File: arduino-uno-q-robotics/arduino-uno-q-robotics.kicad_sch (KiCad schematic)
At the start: 15 parts, among them J1 Conn_02x30_Odd_Even, J2 Conn_02x30_Odd_Even, J3 Connector_FFC-FPC, J4 Connector_FFC-FPC, J5 Conn_02x13_Odd_Even, J6 Conn_02x04_Odd_Even, U1 LSM6DSO32, U2 TCA9803, U4 TCA9803

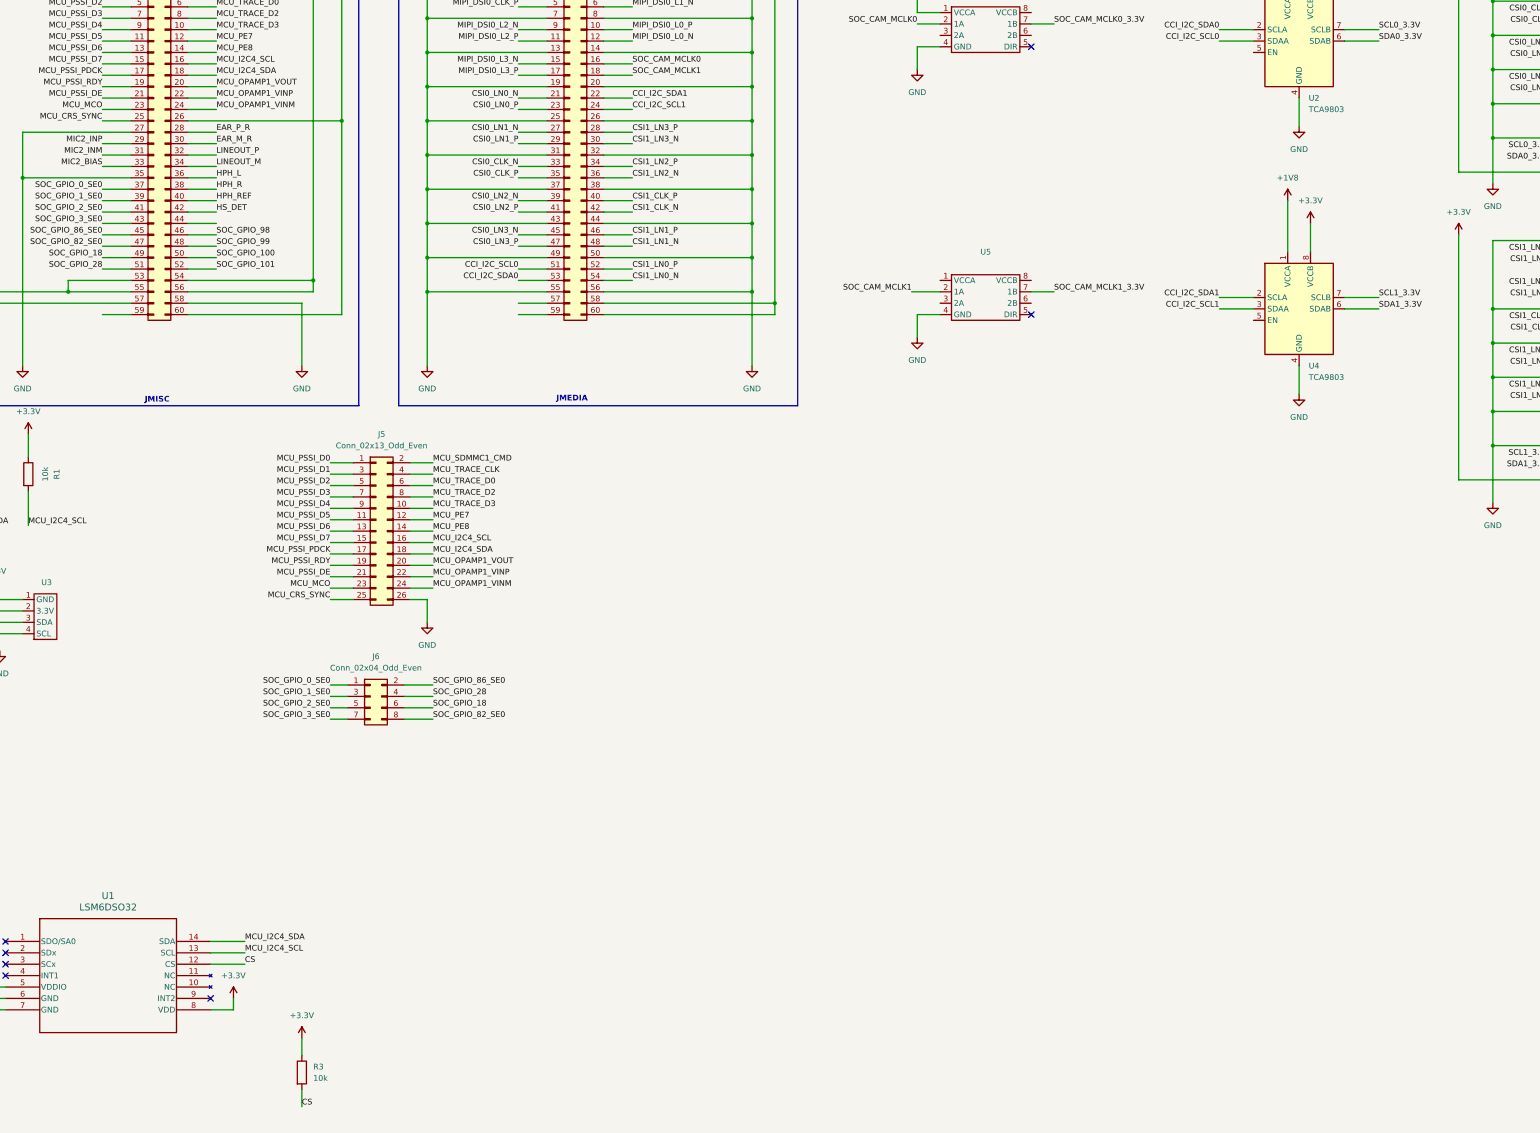
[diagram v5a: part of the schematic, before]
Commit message: Add decoupling capacitors to schematic
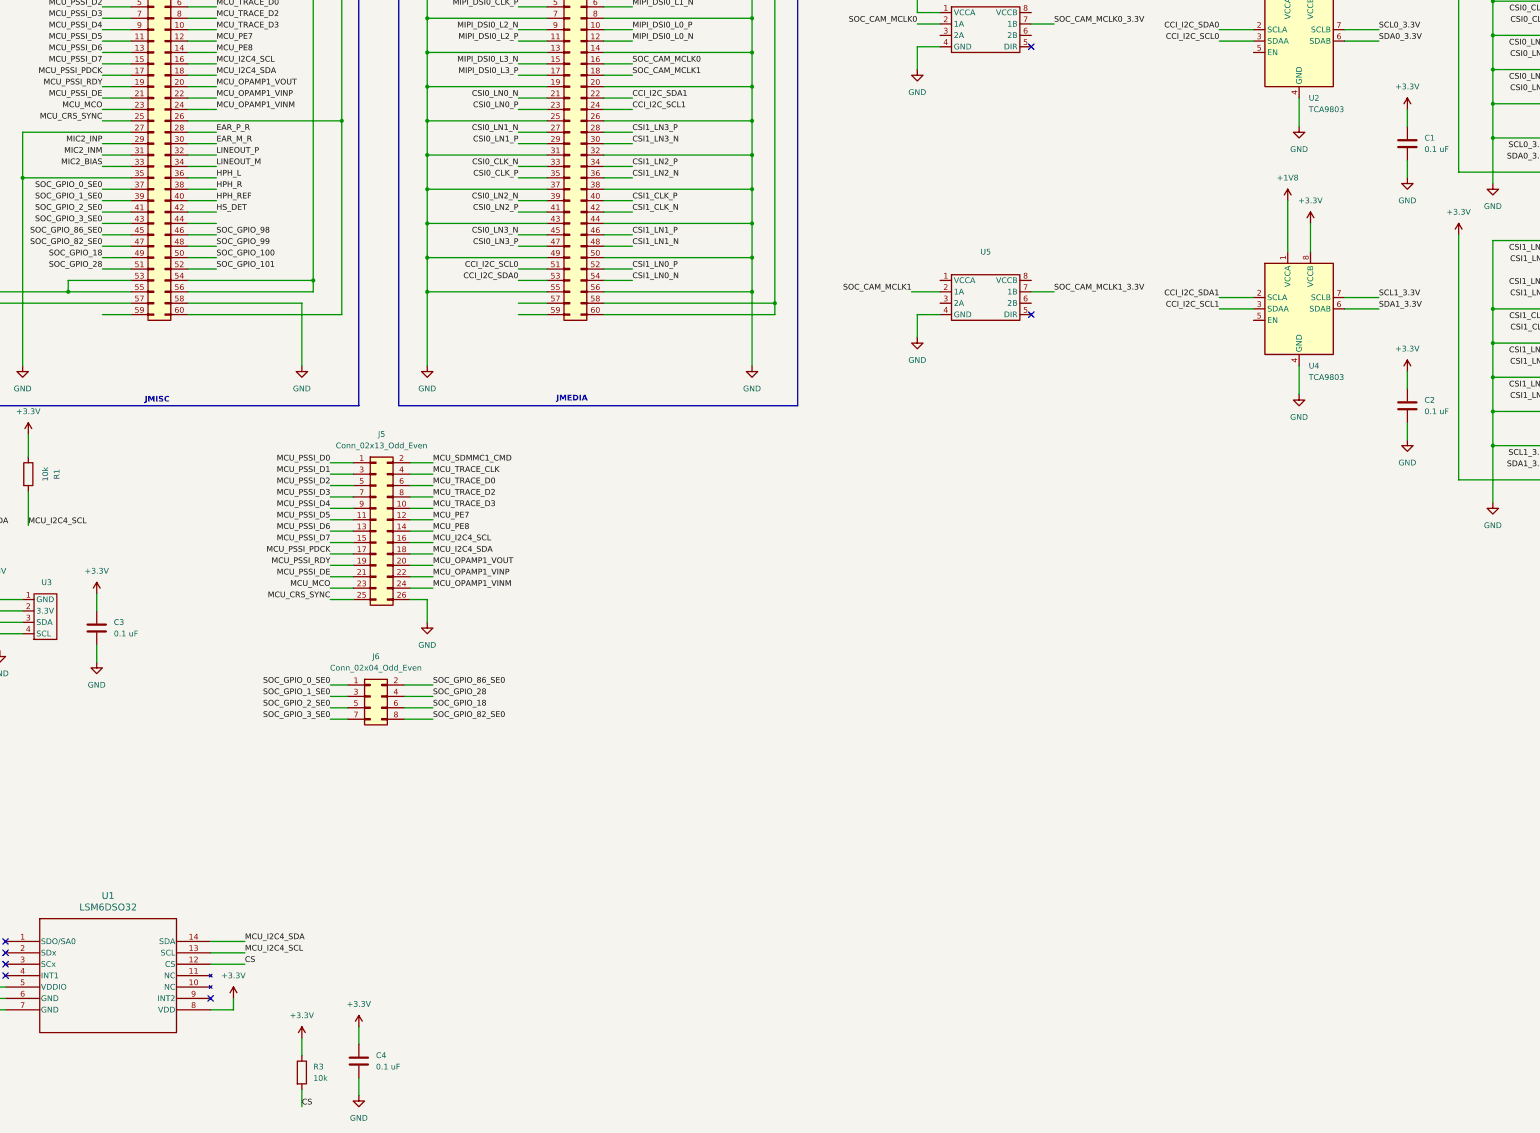
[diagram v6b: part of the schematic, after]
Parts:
- added C1, C2, C3, C4: 0.1 uF, Capacitor_SMD:C_0603_1608Metric_Pad1.08x0.95mm_HandSolder, symbol Device:C
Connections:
- net +3.3V: now also C1.1, C2.1, C3.1, C4.1
- net GND: now also C1.2, C2.2, C3.2, C4.2

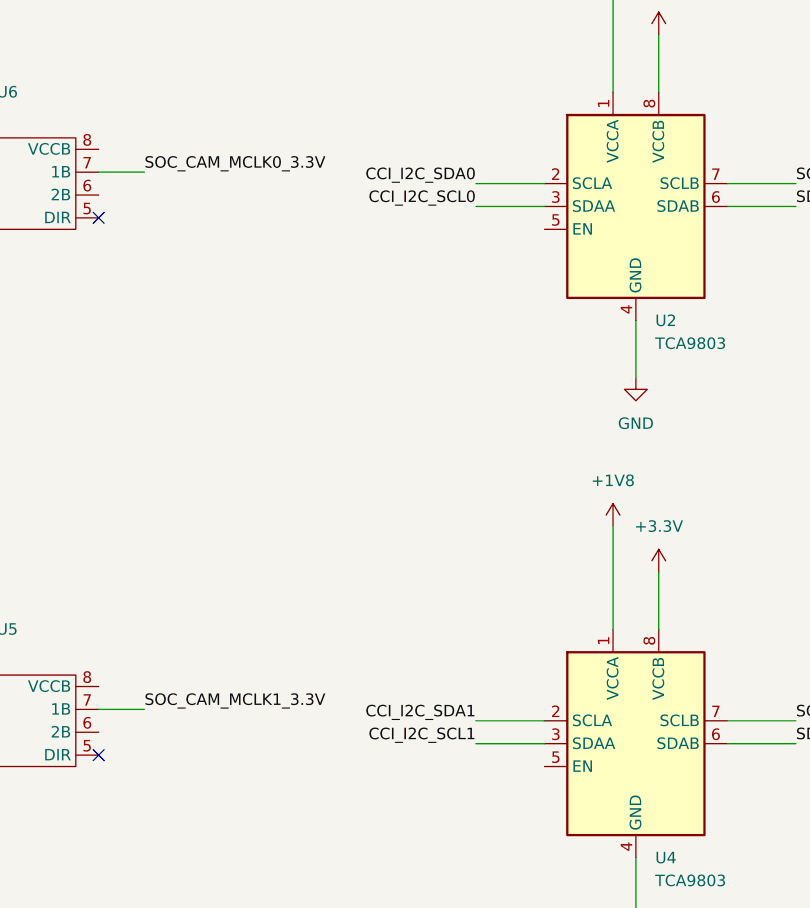
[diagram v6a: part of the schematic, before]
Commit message: Add missing components to PCB editor
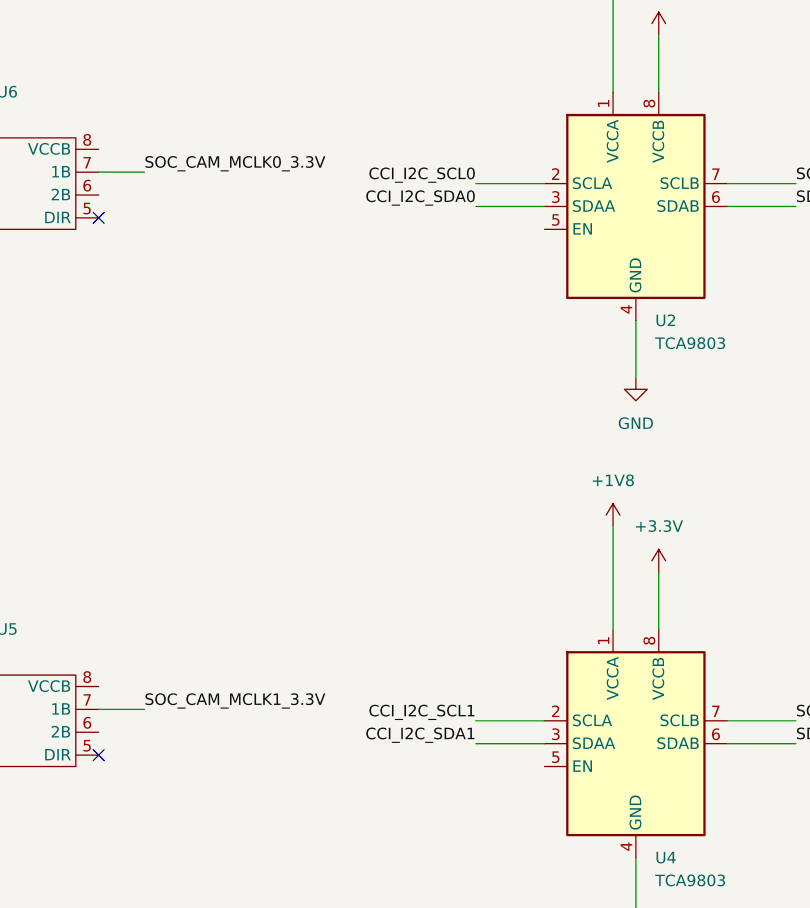
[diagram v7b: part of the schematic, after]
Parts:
- U1: footprint LGA-14L_2P5X3X0P83_STM -> robotics-footprints:LGA-14L_2P5X3X0P83_STM
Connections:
- net CCI_I2C_SCL0: now also U2.2 (SCLA); no longer U2.3 (SDAA)
- net CCI_I2C_SCL1: now also U4.2 (SCLA); no longer U4.3 (SDAA)
- net CCI_I2C_SDA0: now also U2.3 (SDAA); no longer U2.2 (SCLA)
- net CCI_I2C_SDA1: now also U4.3 (SDAA); no longer U4.2 (SCLA)
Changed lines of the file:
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@@
 		)
 	)
-	(label "CCI_I2C_SCL0"
-		(at 302.26 44.45 180)
-		(effects
-			(font
-				(size 1.27 1.27)
-			)
-			(justify right bottom)
-		)
-	)
 	(label "MCU_PSSI_D6"
 		(at 53.34 46.99 180)
@@
 	)
 	(label "CCI_I2C_SCL0"
+		(at 302.26 41.91 180)
+		(effects
+			(font
+				(size 1.27 1.27)
+			)
+			(justify right bottom)
+		)
+	)
+	(label "CCI_I2C_SCL0"
 		(at 146.05 95.25 180)
 		(effects
@@
 		)
 	)
+	(label "CCI_I2C_SDA0"
+		(at 302.26 44.45 180)
+		(effects
+			(font
+				(size 1.27 1.27)
+			)
+			(justify right bottom)
+		)
+	)
 	(label "SOC_GPIO_1_SE0"
 		(at 53.34 80.01 180)
@@
 		)
 	)
-	(label "CCI_I2C_SDA0"
-		(at 302.26 41.91 180)
-		(effects
-			(font
-				(size 1.27 1.27)
-			)
-			(justify right bottom)
-		)
-	)
 	(label "MCU_PSSI_PDCK"
 		(at 53.34 52.07 180)
@@
 		)
 	)
-	(label "CCI_I2C_SDA1"
+	(label "CCI_I2C_SCL1"
 		(at 302.26 101.6 180)
 		(effects
@@
 		)
 	)
-	(label "CCI_I2C_SCL1"
+	(label "CCI_I2C_SDA1"
 		(at 302.26 104.14 180)
 		(effects
@@
 			)
 		)
-		(property "Footprint" "LGA-14L_2P5X3X0P83_STM"
+		(property "Footprint" "robotics-footprints:LGA-14L_2P5X3X0P83_STM"
 			(at 56.642 268.224 0)
 			(effects

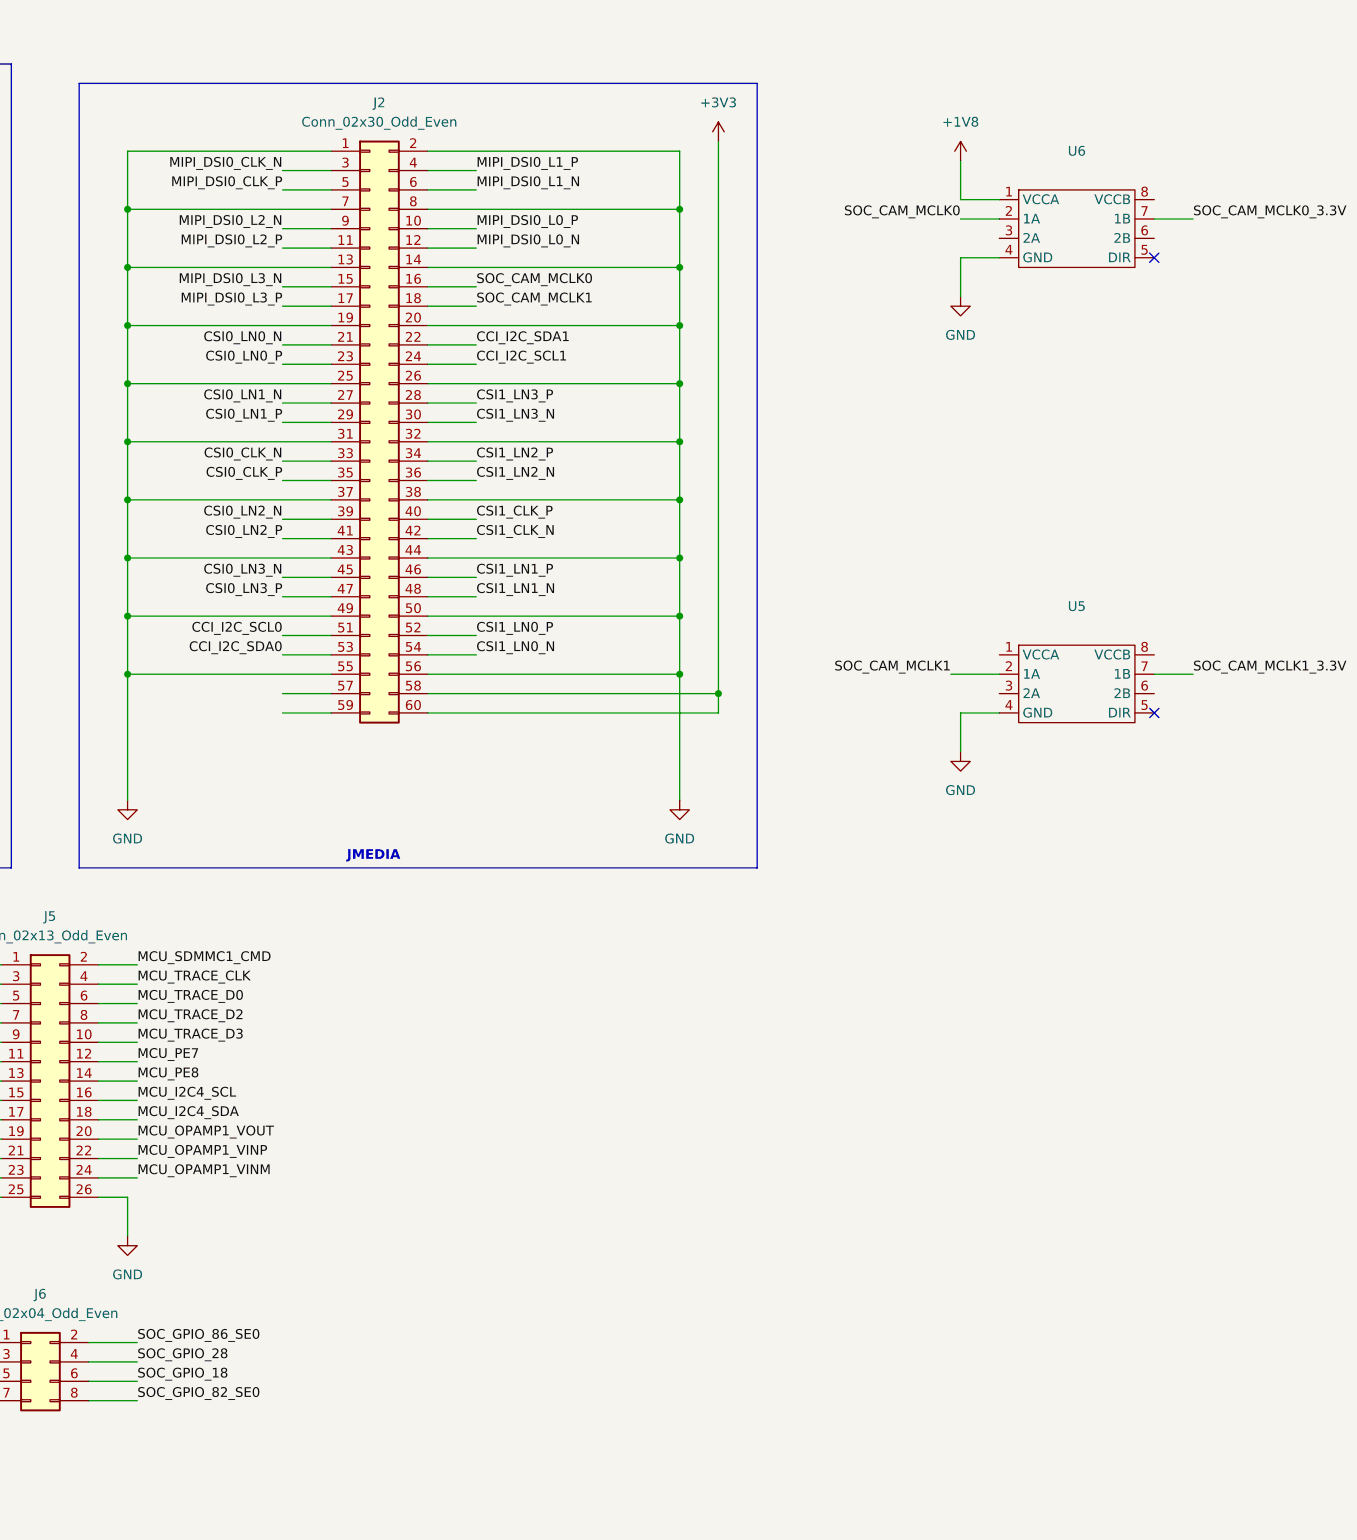
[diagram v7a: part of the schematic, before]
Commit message: Add male header for JMISC ports
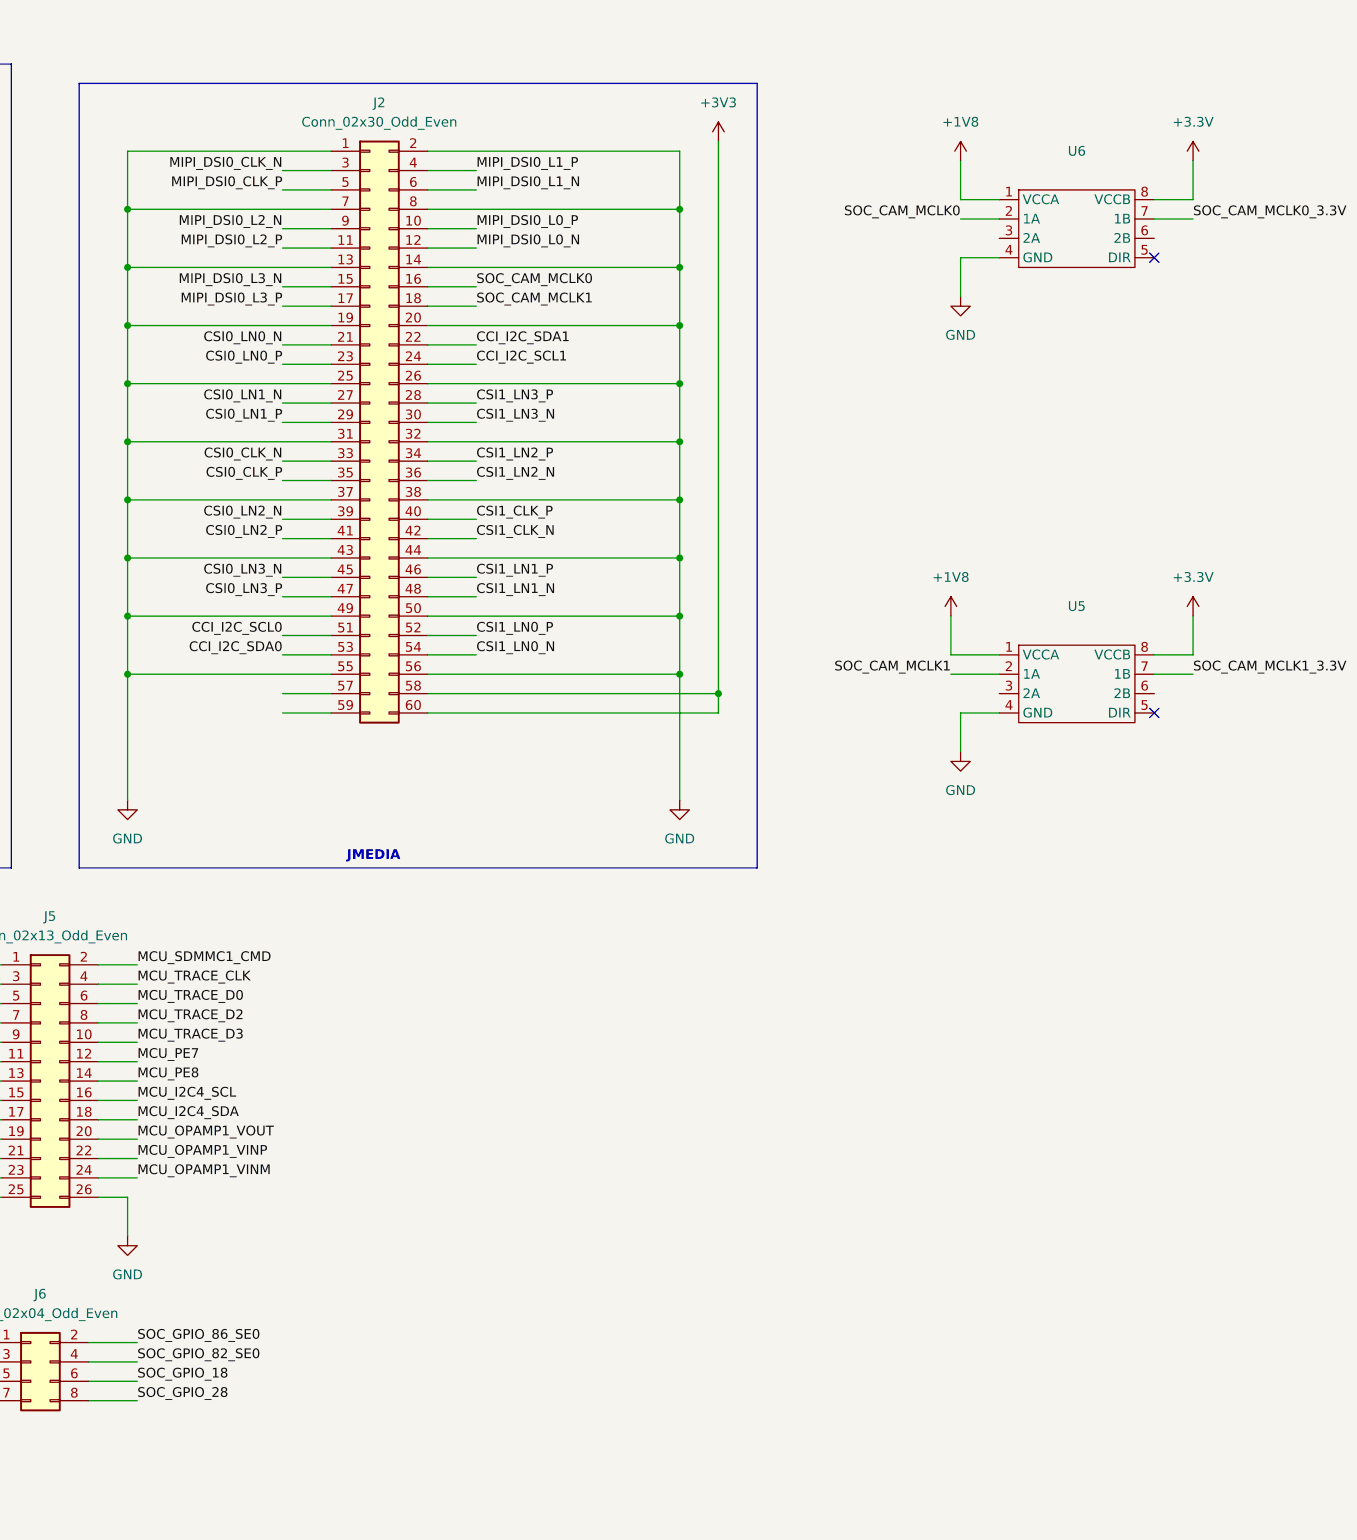
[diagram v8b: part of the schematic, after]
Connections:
- net +1V8: now also U5.1 (VCCA)
- net +3.3V: now also U5.8 (VCCB), U6.8 (VCCB)
- net SOC_GPIO_28: now also J6.8 (Pin_8); no longer J6.4 (Pin_4)
- net SOC_GPIO_82_SE0: now also J6.4 (Pin_4); no longer J6.8 (Pin_8)
